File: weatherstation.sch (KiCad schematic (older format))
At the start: 20 parts

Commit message: Finallized schematic
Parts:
- removed J?: Raspberry_Pi_2_3, symbol Connector:Raspberry_Pi_2_3
- removed R?: 620, symbol Device:R
- removed R?: 100, symbol Device:R
- removed R? (x2): 1k, symbol Device:R
- removed U?: LM741, symbol Amplifier_Operational:LM741
- added D4: LED, symbol Device:LED
- added J1: Conn_02x13_Odd_Even, symbol Connector_Generic:Conn_02x13_Odd_Even
- added J2, J3, J4, J5, J6, J7, J8, J9: Conn_01x02_Male, symbol Connector:Conn_01x02_Male
- added R10, R5, R6: R, symbol Device:R
- added U1: LM741, symbol Amplifier_Operational:LM741
- gave numbers to parts that had none: 14
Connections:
- net labels added: CH1, CH2, CH3, CH4, CH5, CH6, CH7, Dir+, Dir-, DirInput
- net labels removed: Input, Speed+, Speed-, SpeedInput, SpeedOutput, V_REF
- wire segments 68 -> 102
- no-connect marks 26 -> 21
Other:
- note added: "ADC Circuitry\n"
- note added: "ADC Input Pins\n"
- note added: "Raspberry Pi Pins\n"
- note added: "Reference Voltage \nfor the sensor\n\n"
- note added: "Wind Direction Sensor Circuitry\n"
- note removed: "1k/100 = gain of 10\n5 = 500/100\n"
- moved on the sheet: C1, C2, D1, D2, D3, R1, R2, R3, R4, R7, R8, R9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

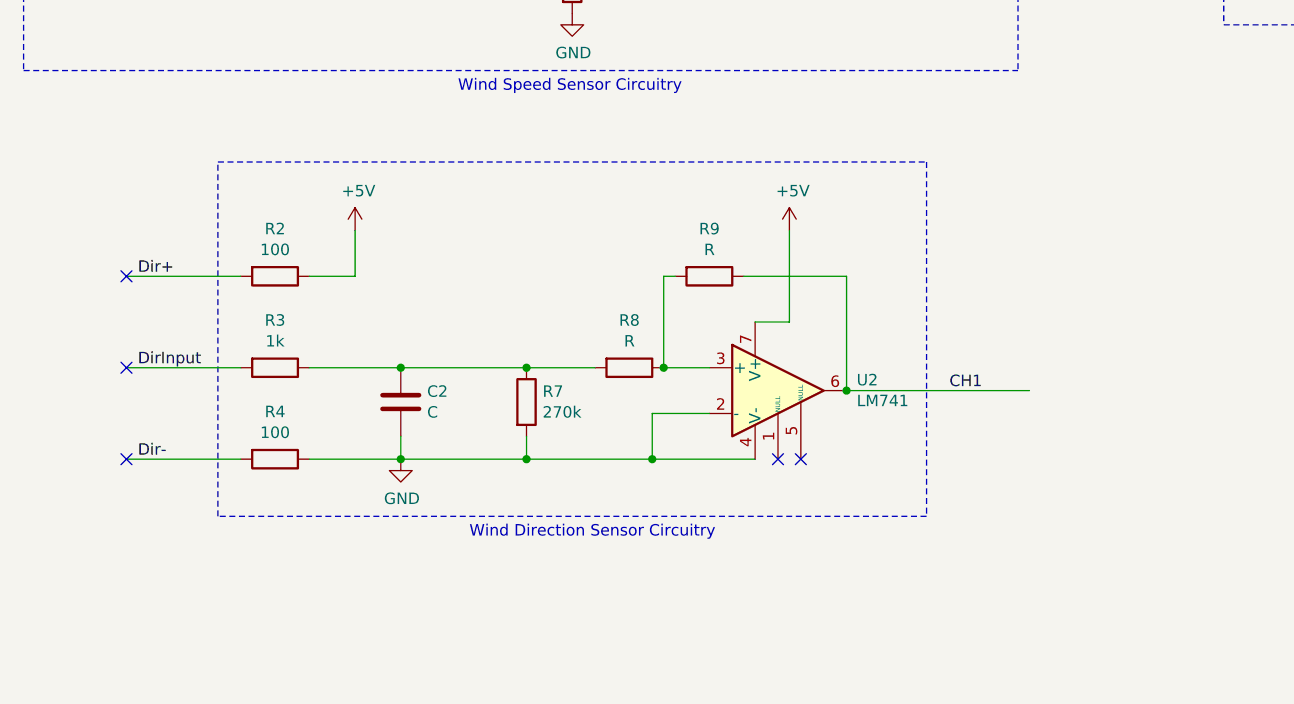
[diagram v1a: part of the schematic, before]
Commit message: Added input for speed direction circuitry
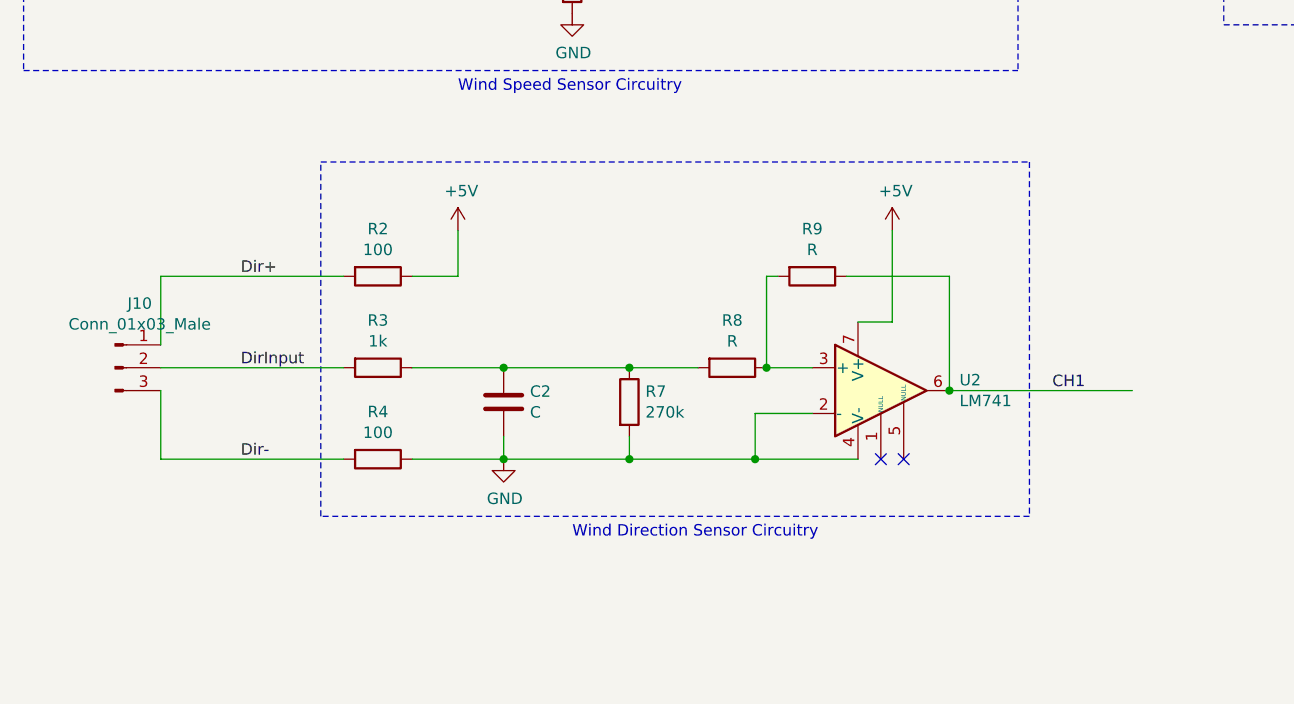
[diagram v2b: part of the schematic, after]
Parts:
- added J10: Conn_01x03_Male, symbol Connector:Conn_01x03_Male
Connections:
- wire segments 102 -> 104
- no-connect marks 21 -> 18
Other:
- moved on the sheet: C2, R2, R3, R4, R7, R8, R9, U2
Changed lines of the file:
@@
 Wire Notes Line
 	7250 600  5900 600
-Text Notes 2600 4950 0    50   ~ 0
+Text Notes 3050 4950 0    50   ~ 0
 Wind Direction Sensor Circuitry\n
 Wire Wire Line
-	4000 3600 4000 4000
+	4450 3600 4450 4000
 $Comp
 L power:+5V #PWR0104
 U 1 1 60C8DBFB
-P 4000 3600
-F 0 "#PWR0104" H 4000 3450 50  0001 C CNN
-F 1 "+5V" H 4015 3773 50  0000 C CNN
-F 2 "" H 4000 3600 50  0001 C CNN
-F 3 "" H 4000 3600 50  0001 C CNN
-	1    4000 3600
-	1    0    0    -1
-$EndComp
-Wire Notes Line
-	4600 3300 4600 4850
-Wire Notes Line
-	1500 3300 4600 3300
-Text Label 4700 4300 0    50   ~ 0
+P 4450 3600
+F 0 "#PWR0104" H 4450 3450 50  0001 C CNN
+F 1 "+5V" H 4465 3773 50  0000 C CNN
+F 2 "" H 4450 3600 50  0001 C CNN
+F 3 "" H 4450 3600 50  0001 C CNN
+	1    4450 3600
+	1    0    0    -1
+$EndComp
+Wire Notes Line
+	5050 3300 5050 4850
+Wire Notes Line
+	1950 3300 5050 3300
+Text Label 5150 4300 0    50   ~ 0
 CH1
-Connection ~ 4250 4300
-Wire Wire Line
-	4250 4300 5050 4300
-NoConn ~ 4050 4600
-NoConn ~ 3950 4600
-Wire Wire Line
-	3400 4600 3850 4600
-Connection ~ 3400 4600
-Wire Wire Line
-	3400 4400 3400 4600
-Wire Wire Line
-	3650 4400 3400 4400
-Connection ~ 2850 4600
-Wire Wire Line
-	2850 4600 3400 4600
-Wire Wire Line
-	2850 4200 3150 4200
-Connection ~ 2850 4200
-Wire Wire Line
-	2300 4200 2850 4200
-Connection ~ 3450 4200
-Wire Wire Line
-	3450 4200 3650 4200
-Wire Wire Line
-	3450 3800 3500 3800
-Wire Wire Line
-	3450 4200 3450 3800
-Wire Wire Line
-	4250 3800 4250 4300
-Wire Wire Line
-	3800 3800 4250 3800
-Wire Wire Line
-	3850 4000 4000 4000
+Connection ~ 4700 4300
+Wire Wire Line
+	4700 4300 5500 4300
+NoConn ~ 4500 4600
+NoConn ~ 4400 4600
+Wire Wire Line
+	3850 4600 4300 4600
+Connection ~ 3850 4600
+Wire Wire Line
+	3850 4400 3850 4600
+Wire Wire Line
+	4100 4400 3850 4400
+Connection ~ 3300 4600
+Wire Wire Line
+	3300 4600 3850 4600
+Wire Wire Line
+	3300 4200 3600 4200
+Connection ~ 3300 4200
+Wire Wire Line
+	2750 4200 3300 4200
+Connection ~ 3900 4200
+Wire Wire Line
+	3900 4200 4100 4200
+Wire Wire Line
+	3900 3800 3950 3800
+Wire Wire Line
+	3900 4200 3900 3800
+Wire Wire Line
+	4700 3800 4700 4300
+Wire Wire Line
+	4250 3800 4700 3800
+Wire Wire Line
+	4300 4000 4450 4000
 $Comp
 L Device:R R9
 U 1 1 60C58AE4
-P 3650 3800
-F 0 "R9" V 3443 3800 50  0000 C CNN
-F 1 "R" V 3534 3800 50  0000 C CNN
-F 2 "" V 3580 3800 50  0001 C CNN
-F 3 "~" H 3650 3800 50  0001 C CNN
-	1    3650 3800
+P 4100 3800
+F 0 "R9" V 3893 3800 50  0000 C CNN
+F 1 "R" V 3984 3800 50  0000 C CNN
+F 2 "" V 4030 3800 50  0001 C CNN
+F 3 "~" H 4100 3800 50  0001 C CNN
+	1    4100 3800
 	0    1    1    0
 $EndComp
@@
 L Device:R R8
 U 1 1 60C57FA4
-P 3300 4200
-F 0 "R8" V 3093 4200 50  0000 C CNN
-F 1 "R" V 3184 4200 50  0000 C CNN
-F 2 "" V 3230 4200 50  0001 C CNN
-F 3 "~" H 3300 4200 50  0001 C CNN
-	1    3300 4200
+P 3750 4200
+F 0 "R8" V 3543 4200 50  0000 C CNN
+F 1 "R" V 3634 4200 50  0000 C CNN
+F 2 "" V 3680 4200 50  0001 C CNN
+F 3 "~" H 3750 4200 50  0001 C CNN
+	1    3750 4200
 	0    1    1    0
 $EndComp
@@
 L Amplifier_Operational:LM741 U2
 U 1 1 60C5380E
-P 3950 4300
-F 0 "U2" H 4294 4346 50  0000 L CNN
-F 1 "LM741" H 4294 4255 50  0000 L CNN
-F 2 "" H 4000 4350 50  0001 C CNN
-F 3 "http://www.ti.com/lit/ds/symlink/lm741.pdf" H 4100 4450 50  0001 C CNN
-	1    3950 4300
-	1    0    0    -1
-$EndComp
-Wire Wire Line
-	2850 4600 2300 4600
-Wire Wire Line
-	2850 4500 2850 4600
-Connection ~ 2300 4200
+P 4400 4300
+F 0 "U2" H 4744 4346 50  0000 L CNN
+F 1 "LM741" H 4744 4255 50  0000 L CNN
+F 2 "" H 4450 4350 50  0001 C CNN
+F 3 "http://www.ti.com/lit/ds/symlink/lm741.pdf" H 4550 4450 50  0001 C CNN
+	1    4400 4300
+	1    0    0    -1
+$EndComp
+Wire Wire Line
+	3300 4600 2750 4600
+Wire Wire Line
+	3300 4500 3300 4600
+Connection ~ 2750 4200
 $Comp
 L Device:R R7
 U 1 1 60C4FF4F
-P 2850 4350
-F 0 "R7" H 2920 4396 50  0000 L CNN
-F 1 "270k" H 2920 4305 50  0000 L CNN
-F 2 "" V 2780 4350 50  0001 C CNN
-F 3 "~" H 2850 4350 50  0001 C CNN
-	1    2850 4350
-	1    0    0    -1
-$EndComp
-Connection ~ 2300 4600
-Wire Wire Line
-	2300 4500 2300 4600
-Wire Wire Line
-	1900 4600 2300 4600
-Wire Wire Line
-	1900 4200 2300 4200
-Wire Wire Line
-	2100 3800 2100 3600
-Wire Wire Line
-	1900 3800 2100 3800
+P 3300 4350
+F 0 "R7" H 3370 4396 50  0000 L CNN
+F 1 "270k" H 3370 4305 50  0000 L CNN
+F 2 "" V 3230 4350 50  0001 C CNN
+F 3 "~" H 3300 4350 50  0001 C CNN
+	1    3300 4350
+	1    0    0    -1
+$EndComp
+Connection ~ 2750 4600
+Wire Wire Line
+	2750 4500 2750 4600
+Wire Wire Line
+	2350 4600 2750 4600
+Wire Wire Line
+	2350 4200 2750 4200
+Wire Wire Line
+	2550 3800 2550 3600
+Wire Wire Line
+	2350 3800 2550 3800
 $Comp
 L power:GND #PWR0105
 U 1 1 60C3F54F
-P 2300 4600
-F 0 "#PWR0105" H 2300 4350 50  0001 C CNN
-F 1 "GND" H 2305 4427 50  0000 C CNN
-F 2 "" H 2300 4600 50  0001 C CNN
-F 3 "" H 2300 4600 50  0001 C CNN
-	1    2300 4600
+P 2750 4600
+F 0 "#PWR0105" H 2750 4350 50  0001 C CNN
+F 1 "GND" H 2755 4427 50  0000 C CNN
+F 2 "" H 2750 4600 50  0001 C CNN
+F 3 "" H 2750 4600 50  0001 C CNN
+	1    2750 4600
 	1    0    0    -1
 $EndComp
@@
 L Device:C C2
 U 1 1 60C3ECA5
-P 2300 4350
-F 0 "C2" H 2415 4396 50  0000 L CNN
-F 1 "C" H 2415 4305 50  0000 L CNN
-F 2 "" H 2338 4200 50  0001 C CNN
-F 3 "~" H 2300 4350 50  0001 C CNN
-	1    2300 4350
+P 2750 4350
+F 0 "C2" H 2865 4396 50  0000 L CNN
+F 1 "C" H 2865 4305 50  0000 L CNN
+F 2 "" H 2788 4200 50  0001 C CNN
+F 3 "~" H 2750 4350 50  0001 C CNN
+	1    2750 4350
 	1    0    0    -1
 $EndComp
@@
 L Device:R R3
 U 1 1 60C2EDA7
-P 1750 4200
-F 0 "R3" V 1543 4200 50  0000 C CNN
-F 1 "1k" V 1634 4200 50  0000 C CNN
-F 2 "" V 1680 4200 50  0001 C CNN
-F 3 "~" H 1750 4200 50  0001 C CNN
-	1    1750 4200
+P 2200 4200
+F 0 "R3" V 1993 4200 50  0000 C CNN
+F 1 "1k" V 2084 4200 50  0000 C CNN
+F 2 "" V 2130 4200 50  0001 C CNN
+F 3 "~" H 2200 4200 50  0001 C CNN
+	1    2200 4200
 	0    1    1    0
 $EndComp
@@
 L Device:R R4
 U 1 1 60C2E51B
-P 1750 4600
-F 0 "R4" V 1543 4600 50  0000 C CNN
-F 1 "100" V 1634 4600 50  0000 C CNN
-F 2 "" V 1680 4600 50  0001 C CNN
-F 3 "~" H 1750 4600 50  0001 C CNN
-	1    1750 4600
+P 2200 4600
+F 0 "R4" V 1993 4600 50  0000 C CNN
+F 1 "100" V 2084 4600 50  0000 C CNN
+F 2 "" V 2130 4600 50  0001 C CNN
+F 3 "~" H 2200 4600 50  0001 C CNN
+	1    2200 4600
 	0    1    1    0
 $EndComp
@@
 L Device:R R2
 U 1 1 60C2DDA7
-P 1750 3800
-F 0 "R2" V 1543 3800 50  0000 C CNN
-F 1 "100" V 1634 3800 50  0000 C CNN
-F 2 "" V 1680 3800 50  0001 C CNN
-F 3 "~" H 1750 3800 50  0001 C CNN
-	1    1750 3800
+P 2200 3800
+F 0 "R2" V 1993 3800 50  0000 C CNN
+F 1 "100" V 2084 3800 50  0000 C CNN
+F 2 "" V 2130 3800 50  0001 C CNN
+F 3 "~" H 2200 3800 50  0001 C CNN
+	1    2200 3800
 	0    1    1    0
 $EndComp
-Text Label 1150 4200 0    50   ~ 0
+Text Label 1600 4200 0    50   ~ 0
 DirInput
-Text Label 1150 4600 0    50   ~ 0
+Text Label 1600 4600 0    50   ~ 0
 Dir-
-Text Label 1150 3800 0    50   ~ 0
+Text Label 1600 3800 0    50   ~ 0
 Dir+
 Wire Notes Line
-	4600 4850 1500 4850
-Wire Notes Line
-	1500 4850 1500 3300
-Wire Wire Line
-	1600 3800 1100 3800
-Wire Wire Line
-	1600 4600 1100 4600
+	5050 4850 1950 4850
+Wire Notes Line
+	1950 4850 1950 3300
 $Comp
 L power:+5V #PWR0113
 U 1 1 60C4BD4E
-P 2100 3600
-F 0 "#PWR0113" H 2100 3450 50  0001 C CNN
-F 1 "+5V" H 2115 3773 50  0000 C CNN
-F 2 "" H 2100 3600 50  0001 C CNN
-F 3 "" H 2100 3600 50  0001 C CNN
-	1    2100 3600
-	1    0    0    -1
-$EndComp
-NoConn ~ 1100 3800
-NoConn ~ 1100 4200
-NoConn ~ 1100 4600
-Wire Wire Line
-	1600 4200 1100 4200
+P 2550 3600
+F 0 "#PWR0113" H 2550 3450 50  0001 C CNN
+F 1 "+5V" H 2565 3773 50  0000 C CNN
+F 2 "" H 2550 3600 50  0001 C CNN
+F 3 "" H 2550 3600 50  0001 C CNN
+	1    2550 3600
+	1    0    0    -1
+$EndComp
 $Comp
 L Connector:Conn_01x02_Male J6
@@
 NoConn ~ 8850 1400
 NoConn ~ 8850 1300
+$Comp
+L Connector:Conn_01x03_Male J10
+U 1 1 60CB4A89
+P 1050 4200
+F 0 "J10" H 1158 4481 50  0000 C CNN
+F 1 "Conn_01x03_Male" H 1158 4390 50  0000 C CNN
+F 2 "" H 1050 4200 50  0001 C CNN
+F 3 "~" H 1050 4200 50  0001 C CNN
+	1    1050 4200
+	1    0    0    -1
+$EndComp
+Wire Wire Line
+	1250 3800 1250 4100
+Wire Wire Line
+	1250 3800 2050 3800
+Wire Wire Line
+	1250 4200 2050 4200
+Wire Wire Line
+	1250 4600 1250 4300
+Wire Wire Line
+	1250 4600 2050 4600
 $EndSCHEMATC
